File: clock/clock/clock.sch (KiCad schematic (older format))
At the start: 44 parts, among them J1 AVR-ISP-6, J10 Conn_01x05_Male, J11 CV_IN, J12 CLOCK_OUT, J13 SUBDIV_OUT, J2 EURORACK_CONN_10, J3 Conn_01x05_Female, J4 Conn_01x05_Male, J5 Conn_01x05_Female, J6 Conn_01x05_Male, J7 Conn_01x05_Female, J8 Conn_01x05_Male, J9 Conn_01x05_Female, SW1 SW_Push, SW2 SW_Push, U1 ATmega328P-PU, U2 L7805, U3 SM460281N, U4 SM460281N, U5 SM460281N, Y1 16MHz

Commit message: update pcb
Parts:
- D3: renamed from D?; footprint Diode_THT:D_DO-35_SOD27_P7.62mm_Horizontal -> Diode_THT:D_T-1_P5.08mm_Horizontal
- R10, R11, R12, R13, R9: renamed from R?; footprint (none) -> Resistor_THT:R_Axial_DIN0207_L6.3mm_D2.5mm_P2.54mm_Vertical
- R14, R15: renamed from R?; footprint (none) -> Resistor_THT:R_Axial_DIN0207_L6.3mm_D2.5mm_P7.62mm_Horizontal
- SW3: renamed from SW?; footprint (none) -> synth:SD-1110
- renumbered R13 to R6, R14 to R7, R15 to R8
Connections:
- net +5V: no longer R10.1, R11.1, R12.1, R9.1
- net AGND: now also R13.1
- net AVCC: now also R10.1, R11.1, R12.1, R9.1
- net GND: no longer R13.1
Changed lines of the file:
@@
 	2600 2950 2700 2950
-Wire Wire Line
-	2700 4150 2450 4150
 Wire Wire Line
 	2450 3050 2700 3050
@@
 Text Label 2700 4950 0    50   ~ 0
 B_LED6
-Text Label 2700 4150 0    50   ~ 0
+Text Label 3150 4150 0    50   ~ 0
 ~RESET
 Text Label 9450 5650 2    50   ~ 0
@@
 Text Label 9500 4100 2    50   ~ 0
 B_LED0
-Text Label 9500 4650 2    50   ~ 0
-B_LED1
-Text Label 9500 4450 2    50   ~ 0
-B_LED2
-Text Label 9500 4750 2    50   ~ 0
-B_LED3
 Text Label 9500 5250 2    50   ~ 0
 B_LED4
@@
 Text Label 9500 3700 2    50   ~ 0
 B_CV_IN
-Text Label 9500 4000 2    50   ~ 0
-B_LED_C1
-Text Label 9500 4550 2    50   ~ 0
-B_LED_C2
-Text Label 9500 4850 2    50   ~ 0
-B_LED_C3
 Text Label 9450 5550 2    50   ~ 0
 B_LED_A
@@
 Text Label 7850 6200 0    50   ~ 0
 AGND
-Text Label 5250 5200 1    50   ~ 0
+Text Label 6450 3550 1    50   ~ 0
 AVCC
 Text Label 4100 5200 1    50   ~ 0
@@
 AVCC
 $Comp
-L Device:R R13
+L Device:R R6
 U 1 1 63915D28
 P 2850 3850
-F 0 "R13" V 2800 3600 50  0000 L CNN
+F 0 "R6" V 2800 3600 50  0000 L CNN
 F 1 "1K" V 2850 3800 50  0000 L CNN
 F 2 "Resistor_THT:R_Axial_DIN0207_L6.3mm_D2.5mm_P2.54mm_Vertical" V 2780 3850 50  0001 C CNN
@@
 $EndComp
 $Comp
-L Device:R R14
+L Device:R R7
 U 1 1 63916389
 P 2850 3950
-F 0 "R14" V 2800 3700 50  0000 L CNN
+F 0 "R7" V 2800 3700 50  0000 L CNN
 F 1 "1K" V 2850 3900 50  0000 L CNN
 F 2 "Resistor_THT:R_Axial_DIN0207_L6.3mm_D2.5mm_P2.54mm_Vertical" V 2780 3950 50  0001 C CNN
@@
 $EndComp
 $Comp
-L Device:R R15
+L Device:R R8
 U 1 1 639166C2
 P 2850 4050
-F 0 "R15" V 2800 3800 50  0000 L CNN
+F 0 "R8" V 2800 3800 50  0000 L CNN
 F 1 "1K" V 2850 4000 50  0000 L CNN
 F 2 "Resistor_THT:R_Axial_DIN0207_L6.3mm_D2.5mm_P2.54mm_Vertical" V 2780 4050 50  0001 C CNN
@@
 	7150 5100 6950 5100
 $Comp
-L Diode:1N4148 D?
+L Diode:1N4148 D3
 U 1 1 6342DA40
 P 7600 5200
-F 0 "D?" H 7600 4983 50  0000 C CNN
+F 0 "D3" H 7600 4983 50  0000 C CNN
 F 1 "1N4148" H 7600 5074 50  0000 C CNN
-F 2 "Diode_THT:D_DO-35_SOD27_P7.62mm_Horizontal" H 7600 5025 50  0001 C CNN
+F 2 "Diode_THT:D_T-1_P5.08mm_Horizontal" H 7600 5025 50  0001 C CNN
 F 3 "https://assets.nexperia.com/documents/data-sheet/1N4148_1N4448.pdf" H 7600 5200 50  0001 C CNN
 	1    7600 5200
@@
 $EndComp
 $Comp
-L Device:R R?
+L Device:R R14
 U 1 1 6342F08D
 P 7850 5450
-F 0 "R?" H 7920 5496 50  0000 L CNN
+F 0 "R14" H 7920 5496 50  0000 L CNN
 F 1 "180K" H 7920 5405 50  0000 L CNN
-F 2 "" V 7780 5450 50  0001 C CNN
+F 2 "Resistor_THT:R_Axial_DIN0207_L6.3mm_D2.5mm_P7.62mm_Horizontal" V 7780 5450 50  0001 C CNN
 F 3 "~" H 7850 5450 50  0001 C CNN
 	1    7850 5450
@@
 $EndComp
 $Comp
-L Device:R R?
+L Device:R R15
 U 1 1 6342F86A
 P 7850 5900
-F 0 "R?" H 7920 5946 50  0000 L CNN
+F 0 "R15" H 7920 5946 50  0000 L CNN
 F 1 "100K" H 7920 5855 50  0000 L CNN
-F 2 "" V 7780 5900 50  0001 C CNN
+F 2 "Resistor_THT:R_Axial_DIN0207_L6.3mm_D2.5mm_P7.62mm_Horizontal" V 7780 5900 50  0001 C CNN
 F 3 "~" H 7850 5900 50  0001 C CNN
 	1    7850 5900
@@
 bound input CV to 0-5V
 $Comp
-L Switch:SW_Coded_SH-7050 SW?
+L Switch:SW_Coded_SH-7050 SW3
 U 1 1 6348F991
 P 5500 3950
-F 0 "SW?" H 5557 4417 50  0000 C CNN
+F 0 "SW3" H 5557 4417 50  0000 C CNN
 F 1 "SW_Coded_SH-7050" H 5557 4326 50  0000 C CNN
-F 2 "" H 5200 3500 50  0001 L CNN
+F 2 "synth:SD-1110" H 5200 3500 50  0001 L CNN
 F 3 "https://www.nidec-copal-electronics.com/e/catalog/switch/sh-7000.pdf" H 5500 3950 50  0001 C CNN
 	1    5500 3950
@@
 $EndComp
 $Comp
-L Device:R R?
+L Device:R R9
 U 1 1 634912AF
 P 6250 3850
-F 0 "R?" V 6250 4150 50  0000 C CNN
+F 0 "R9" V 6250 4150 50  0000 C CNN
 F 1 "120K" V 6250 3850 50  0000 C CNN
-F 2 "" V 6180 3850 50  0001 C CNN
+F 2 "Resistor_THT:R_Axial_DIN0207_L6.3mm_D2.5mm_P2.54mm_Vertical" V 6180 3850 50  0001 C CNN
 F 3 "~" H 6250 3850 50  0001 C CNN
 	1    6250 3850
@@
 $EndComp
 $Comp
-L Device:R R?
+L Device:R R13
 U 1 1 63491618
 P 6850 3900
-F 0 "R?" H 6780 3854 50  0000 R CNN
+F 0 "R13" H 6780 3854 50  0000 R CNN
 F 1 "68k" H 6780 3945 50  0000 R CNN
-F 2 "" V 6780 3900 50  0001 C CNN
+F 2 "Resistor_THT:R_Axial_DIN0207_L6.3mm_D2.5mm_P2.54mm_Vertical" V 6780 3900 50  0001 C CNN
 F 3 "~" H 6850 3900 50  0001 C CNN
 	1    6850 3900
 	-1   0    0    1
 $EndComp
-$Comp
-L power:+5V #PWR?
-U 1 1 63492617
-P 6450 3550
-F 0 "#PWR?" H 6450 3400 50  0001 C CNN
-F 1 "+5V" H 6465 3723 50  0000 C CNN
-F 2 "" H 6450 3550 50  0001 C CNN
-F 3 "" H 6450 3550 50  0001 C CNN
-	1    6450 3550
-	1    0    0    -1
-$EndComp
-$Comp
-L power:GND #PWR?
-U 1 1 6349300A
-P 6850 4250
-F 0 "#PWR?" H 6850 4000 50  0001 C CNN
-F 1 "GND" H 6855 4077 50  0000 C CNN
-F 2 "" H 6850 4250 50  0001 C CNN
-F 3 "" H 6850 4250 50  0001 C CNN
-	1    6850 4250
-	1    0    0    -1
-$EndComp
 Wire Wire Line
 	6850 4250 6850 4050
@@
 Connection ~ 6850 3750
 $Comp
-L Device:R R?
+L Device:R R10
 U 1 1 635B6095
 P 6250 3950
-F 0 "R?" V 6250 4250 50  0000 C CNN
+F 0 "R10" V 6250 4250 50  0000 C CNN
 F 1 "220K" V 6250 3950 50  0000 C CNN
-F 2 "" V 6180 3950 50  0001 C CNN
+F 2 "Resistor_THT:R_Axial_DIN0207_L6.3mm_D2.5mm_P2.54mm_Vertical" V 6180 3950 50  0001 C CNN
 F 3 "~" H 6250 3950 50  0001 C CNN
 	1    6250 3950
@@
 $EndComp
 $Comp
-L Device:R R?
+L Device:R R11
 U 1 1 635B63E3
 P 6250 4050
-F 0 "R?" V 6250 4350 50  0000 C CNN
+F 0 "R11" V 6250 4350 50  0000 C CNN
 F 1 "470K" V 6250 4050 50  0000 C CNN
-F 2 "" V 6180 4050 50  0001 C CNN
+F 2 "Resistor_THT:R_Axial_DIN0207_L6.3mm_D2.5mm_P2.54mm_Vertical" V 6180 4050 50  0001 C CNN
 F 3 "~" H 6250 4050 50  0001 C CNN
 	1    6250 4050
@@
 $EndComp
 $Comp
-L Device:R R?
+L Device:R R12
 U 1 1 635B6785
 P 6250 4150
-F 0 "R?" V 6250 4450 50  0000 C CNN
+F 0 "R12" V 6250 4450 50  0000 C CNN
 F 1 "1M" V 6250 4150 50  0000 C CNN
-F 2 "" V 6180 4150 50  0001 C CNN
+F 2 "Resistor_THT:R_Axial_DIN0207_L6.3mm_D2.5mm_P2.54mm_Vertical" V 6180 4150 50  0001 C CNN
 F 3 "~" H 6250 4150 50  0001 C CNN
 	1    6250 4150
 	0    1    1    0
 $EndComp
+Wire Wire Line
+	2450 4150 3150 4150
+Text Label 6850 4250 0    50   ~ 0
+AGND
+Text Label 5250 5200 1    50   ~ 0
+AVCC
+Text Label 9500 4450 2    50   ~ 0
+B_LED2
+Text Label 9500 4650 2    50   ~ 0
+B_LED1
+Text Label 9500 4750 2    50   ~ 0
+B_LED3
+Text Label 9500 4000 2    50   ~ 0
+B_LED_C1
+Text Label 9500 4550 2    50   ~ 0
+B_LED_C2
+Text Label 9500 4850 2    50   ~ 0
+B_LED_C3
 $EndSCHEMATC

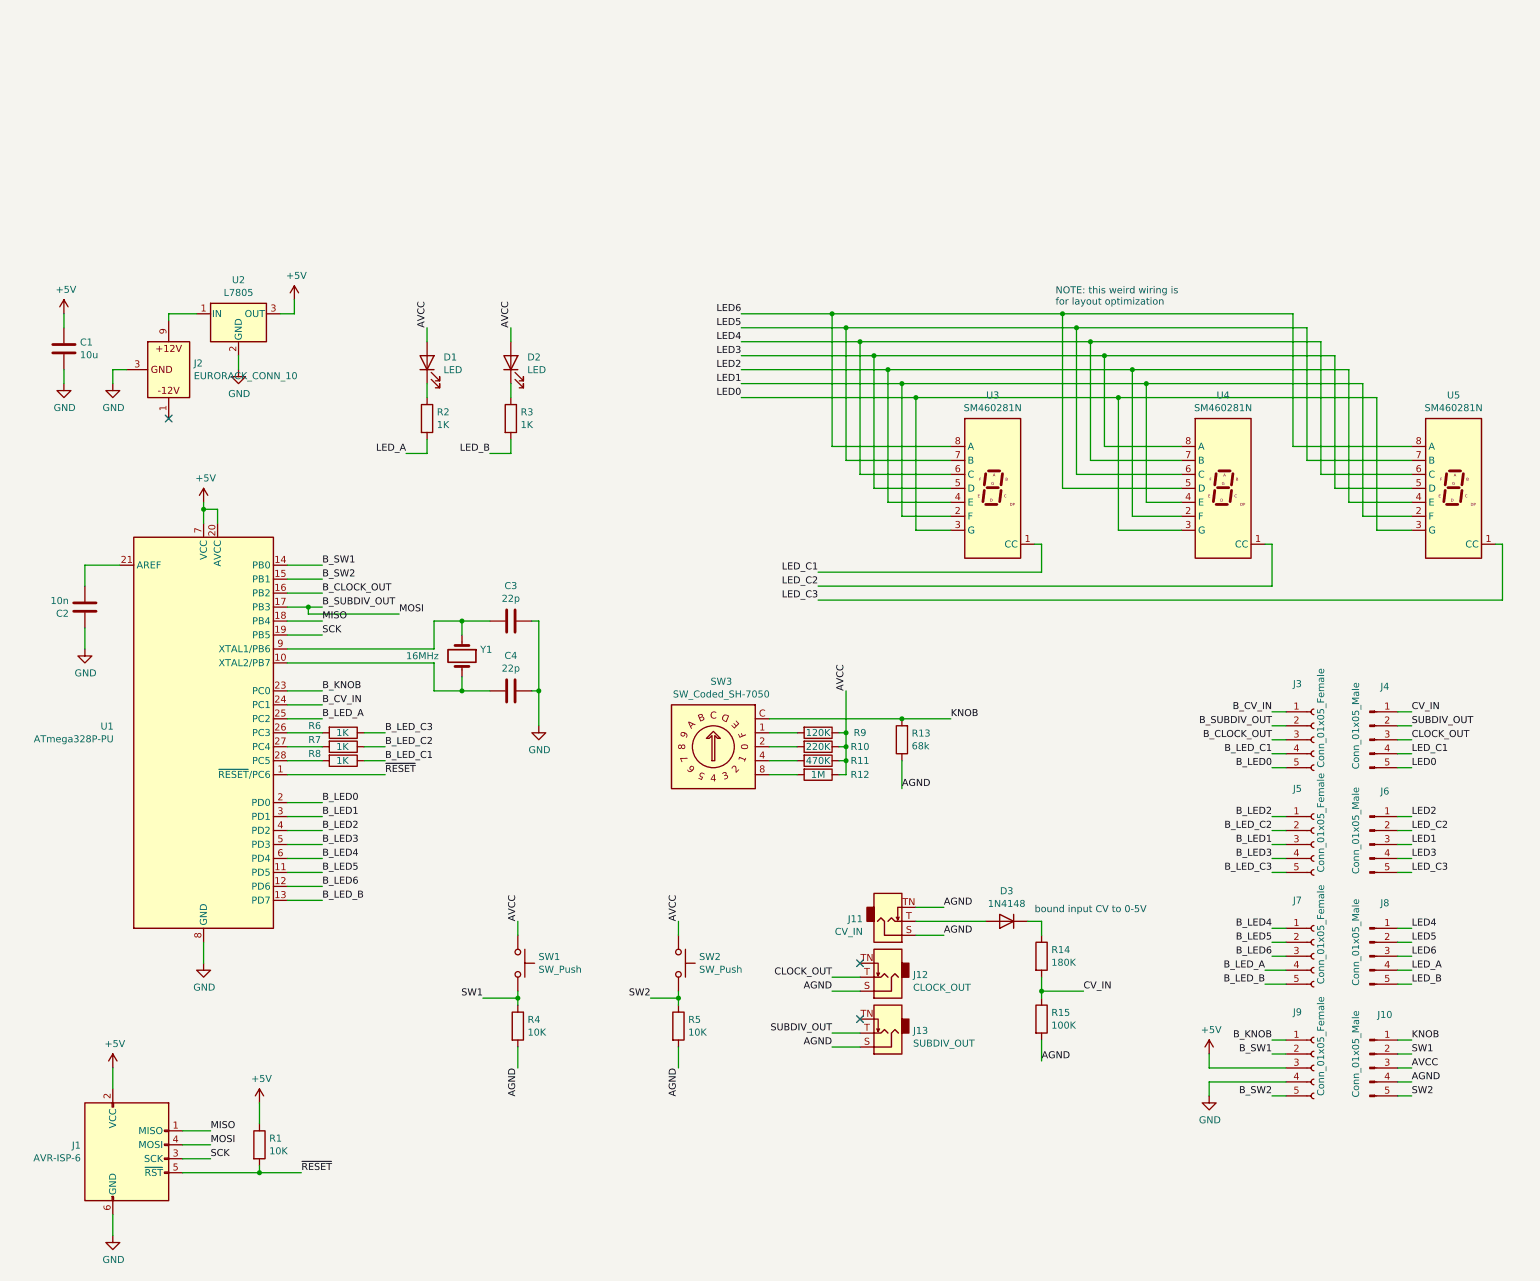
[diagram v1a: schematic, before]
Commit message: redesign pcb around rotary encoder
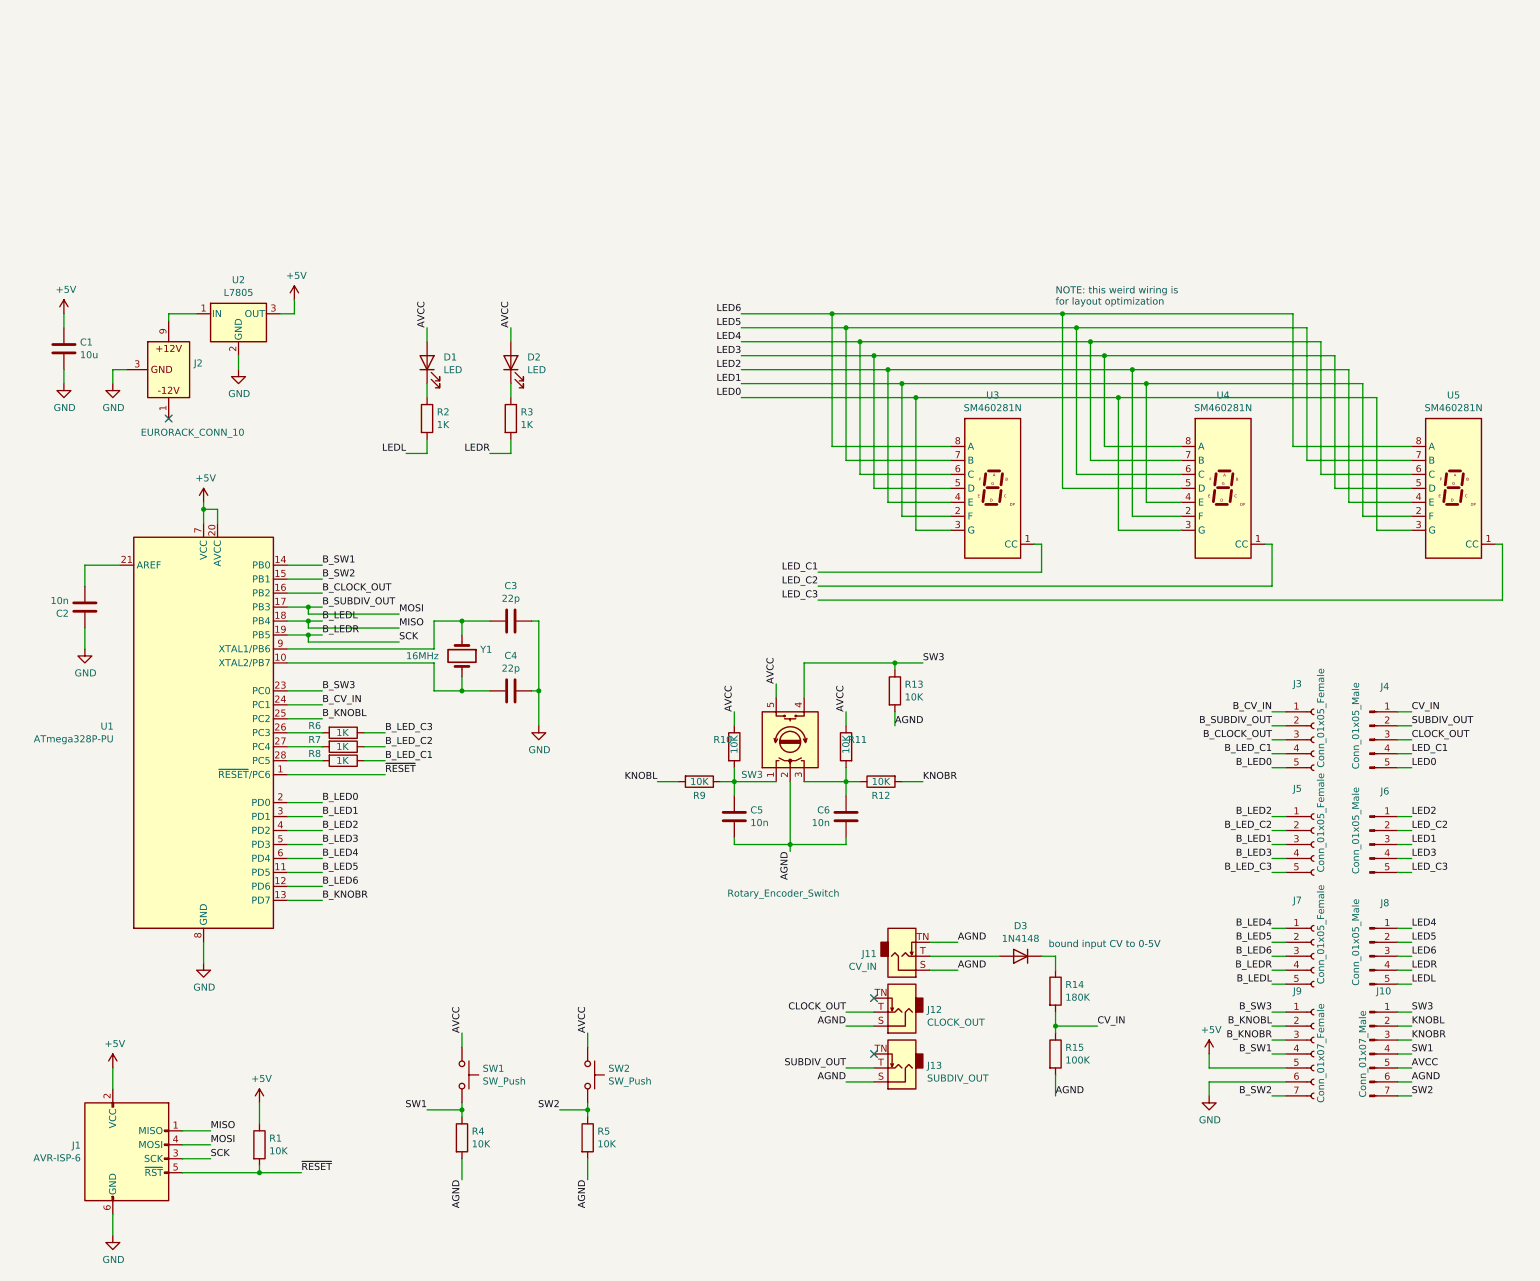
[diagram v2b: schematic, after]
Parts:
- removed J10: Conn_01x05_Male, Connector_PinHeader_2.54mm:PinHeader_1x05_P2.54mm_Vertical, symbol Connector:Conn_01x05_Male
- removed J9: Conn_01x05_Female, Connector_PinSocket_2.54mm:PinSocket_1x05_P2.54mm_Vertical, symbol Connector:Conn_01x05_Female
- removed SW3: SW_Coded_SH-7050, synth:SD-1110, symbol Switch:SW_Coded_SH-7050
- added C5, C6: 10n, Capacitor_THT:C_Rect_L7.0mm_W3.5mm_P5.00mm, symbol Device:C
- added J10: Conn_01x07_Male, Connector_PinHeader_2.54mm:PinHeader_1x07_P2.54mm_Vertical, symbol Connector:Conn_01x07_Male
- added J9: Conn_01x07_Female, Connector_PinSocket_2.54mm:PinSocket_1x07_P2.54mm_Vertical, symbol Connector:Conn_01x07_Female
- added SW3: Rotary_Encoder_Switch, synth:RotaryEncoder_Bourns_PEC11H_Vertical_Switch, symbol Device:Rotary_Encoder_Switch
- R1: footprint Resistor_THT:R_Axial_DIN0207_L6.3mm_D2.5mm_P2.54mm_Vertical -> Resistor_THT:R_Axial_DIN0207_L6.3mm_D2.5mm_P5.08mm_Vertical
- R10: value 220K -> 10K
- R11: value 470K -> 10K
- R12: value 1M -> 10K
- R13: value 68k -> 10K
- R9: value 120K -> 10K
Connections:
- net KNOB is gone; now on net AGND: R13.2
- net +5V: now also J9.5 (Pin_5)
- net AGND: now also C5.2, C6.2, J10.6 (Pin_6), SW3.2 (C); no longer R13.1
- net AVCC: now also J10.5 (Pin_5), SW3.5 (S1); no longer R12.1, R9.1
- net B_SW1: now also J9.4 (Pin_4)
- net B_SW2: now also J9.7 (Pin_7)
- net GND: now also J9.6 (Pin_6)
- net SW1: now also J10.4 (Pin_4)
- net SW2: now also J10.7 (Pin_7)
- net KNOBL: now reaches R9.2
- net KNOBL: now also J10.2 (Pin_2)
- net at R10.2: now also R9.1, C5.1, SW3.1 (A)
- net at R11.2: now also R12.1, C6.1, SW3.3 (B)
- net KNOBR: now reaches R12.2
- net KNOBR: now also J10.3 (Pin_3)
- net B_KNOB renamed B_SW3
- net B_SW3: now also J9.1 (Pin_1)
- net B_LED_A renamed B_KNOBL
- net B_KNOBL: now also J9.2 (Pin_2); no longer J7.4 (Pin_4)
- net B_LED_B renamed B_KNOBR
- net B_KNOBR: now also J9.3 (Pin_3); no longer J7.5 (Pin_5)
- net LED_A renamed LEDL
- net LEDL: now also J8.5 (Pin_5); no longer J8.4 (Pin_4)
- net LED_B renamed LEDR
- net LEDR: now also J8.4 (Pin_4); no longer J8.5 (Pin_5)
- net MISO renamed B_LEDL
- net B_LEDL: now also J7.5 (Pin_5)
- net SCK renamed B_LEDR
- net B_LEDR: now also J7.4 (Pin_4)
- new net SW3: J10.1 (Pin_1), R13.1, SW3.4 (S2)
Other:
- moved on the sheet: D3, J11, J12, J13, R14, R15, R4, R5, SW1, SW2

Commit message: make a bit more space
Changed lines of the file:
@@
 Wire Wire Line
 	9500 5650 9600 5650
+Connection ~ 2650 -1300
 $EndSCHEMATC

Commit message: testing rotary encoder
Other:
- note added: "top-bottom board interface"
- note removed: "bound input CV to 0-5V"
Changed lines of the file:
@@
 Text Label 3250 3200 0    50   ~ 0
 SCK
-Text Label 2700 3750 0    50   ~ 0
-B_KNOBL
 Wire Wire Line
 	2700 3550 2450 3550
@@
 Text Label 2700 4350 0    50   ~ 0
 B_LED0
-Text Label 2700 4450 0    50   ~ 0
-B_LED1
-Text Label 2700 4550 0    50   ~ 0
-B_LED2
 Text Label 2700 4650 0    50   ~ 0
 B_LED3
@@
 Text Label 7250 5550 0    50   ~ 0
 AGND
-Text Notes 7900 5400 0    50   ~ 0
-bound input CV to 0-5V
 Text Label 5100 4200 2    50   ~ 0
 KNOBL
@@
 U 1 1 63860657
 P 5650 3950
-F 0 "R10" H 5500 4000 50  0000 L CNN
-F 1 "10K" V 5650 3900 50  0000 L CNN
+F 0 "R10" H 5450 4000 50  0000 L CNN
+F 1 "10K" H 5450 3900 50  0000 L CNN
 F 2 "Resistor_THT:R_Axial_DIN0207_L6.3mm_D2.5mm_P2.54mm_Vertical" V 5580 3950 50  0001 C CNN
 F 3 "~" H 5650 3950 50  0001 C CNN
@@
 P 5400 4200
 F 0 "R9" V 5500 4200 50  0000 C CNN
-F 1 "10K" V 5400 4200 50  0000 C CNN
+F 1 "10K" V 5600 4200 50  0000 C CNN
 F 2 "Resistor_THT:R_Axial_DIN0207_L6.3mm_D2.5mm_P2.54mm_Vertical" V 5330 4200 50  0001 C CNN
 F 3 "~" H 5400 4200 50  0001 C CNN
@@
 U 1 1 638F4837
 P 6450 3950
-F 0 "R11" H 6300 4000 50  0000 L CNN
-F 1 "10K" V 6450 3900 50  0000 L CNN
+F 0 "R11" H 6250 4000 50  0000 L CNN
+F 1 "10K" H 6250 3900 50  0000 L CNN
 F 2 "Resistor_THT:R_Axial_DIN0207_L6.3mm_D2.5mm_P2.54mm_Vertical" V 6380 3950 50  0001 C CNN
 F 3 "~" H 6450 3950 50  0001 C CNN
@@
 P 6700 4200
 F 0 "R12" V 6800 4200 50  0000 C CNN
-F 1 "10K" V 6700 4200 50  0000 C CNN
+F 1 "10K" V 6900 4200 50  0000 C CNN
 F 2 "Resistor_THT:R_Axial_DIN0207_L6.3mm_D2.5mm_P2.54mm_Vertical" V 6630 4200 50  0001 C CNN
 F 3 "~" H 6700 4200 50  0001 C CNN
@@
 Text Label 9500 6050 2    50   ~ 0
 B_KNOBR
-Text Label 2700 5050 0    50   ~ 0
-B_KNOBR
 Wire Wire Line
 	3250 3100 2600 3100
@@
 Wire Wire Line
 	2600 3150 2700 3150
-Text Label 2700 3550 0    50   ~ 0
-B_SW3
 Text Label 5950 3500 1    50   ~ 0
 AVCC
@@
 Wire Wire Line
 	9500 5650 9600 5650
-Connection ~ 2650 -1300
+Text Label 2700 3750 0    50   ~ 0
+B_KNOBL
+Text Label 2700 4550 0    50   ~ 0
+B_LED2
+Text Label 2700 4450 0    50   ~ 0
+B_LED1
+Text Label 2700 3550 0    50   ~ 0
+B_SW3
+Text Label 2700 5050 0    50   ~ 0
+B_KNOBR
+Text Notes 9550 3300 0    50   ~ 0
+top-bottom board interface
 $EndSCHEMATC

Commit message: fix PCB
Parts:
- removed R12, R9: 10K, Resistor_THT:R_Axial_DIN0207_L6.3mm_D2.5mm_P2.54mm_Vertical, symbol Device:R
- SW3: footprint synth:RotaryEncoder_Bourns_PEC11H_Vertical_Switch -> synth:RotaryEncoder_Bourns_PEC11R_Vertical_Switch
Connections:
- net AGND: now also D1.1 (K), D2.1 (K)
- net AVCC: no longer D1.2 (A), D2.2 (A)
- net B_KNOBR: now also J9.1 (Pin_1), U1.23 (PC0); no longer J9.3 (Pin_3), U1.13 (PD7)
- net B_SW3: now also J9.3 (Pin_3), U1.13 (PD7); no longer J9.1 (Pin_1), U1.23 (PC0)
- net KNOBL: now also C5.1, R10.2, SW3.1 (A)
- net KNOBR: now also C6.1, J10.1 (Pin_1), R11.2, SW3.3 (B); no longer J10.3 (Pin_3)
- net SW3: now also J10.3 (Pin_3); no longer J10.1 (Pin_1)
- net at R2.1: now also D1.2 (A); no longer D1.1 (K)
- net at R3.1: now also D2.2 (A); no longer D2.1 (K)
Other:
- moved on the sheet: D1, D2, R2, R3

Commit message: beautify schematic
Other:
- note added: "7-segment display"
- note added: "IO jacks"
- note added: "Microprocessor"
- note added: "NOTE: this weird wiring for digit 2 is\nfor PCB layout optimization, corrected in software"
- note added: "Power supply"
- note added: "Programming headers"
- note removed: "NOTE: this weird wiring is\nfor layout optimization"
- moved on the sheet: C5, C6, D1, D2, D3, J1, J10, J11, J12, J13, J3, J4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
